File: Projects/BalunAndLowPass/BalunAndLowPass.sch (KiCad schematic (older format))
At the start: 16 parts, among them J1 SMA-J-P-H-ST-EM1, J2 SMA-J-P-H-ST-EM1, J3 SMA-J-P-H-ST-EM1, J4 SMA-J-P-H-ST-EM1, J5 SMA-J-P-H-ST-EM1, J6 SMA-J-P-H-ST-EM1

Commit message: post board review they are all ready to order
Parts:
- added L11, L22: 470nH, Inductor_SMD:L_0805_2012Metric, symbol Device:L
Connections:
- net I_Filtered: now also L11.1; no longer L1.1
- net Q_Filtered: now also L22.1; no longer L2.1
- new net: L1.1, L11.2
- new net: L2.1, L22.2
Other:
- moved on the sheet: C2, C4, J5, J6
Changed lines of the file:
@@
 L Device:C C2
 U 1 1 60232846
-P 5800 2300
-F 0 "C2" H 5915 2346 50  0000 L CNN
-F 1 "160pF" H 5915 2255 50  0000 L CNN
-F 2 "Capacitor_SMD:C_0805_2012Metric" H 5838 2150 50  0001 C CNN
-F 3 "~" H 5800 2300 50  0001 C CNN
-	1    5800 2300
+P 6350 2300
+F 0 "C2" H 6465 2346 50  0000 L CNN
+F 1 "160pF" H 6465 2255 50  0000 L CNN
+F 2 "Capacitor_SMD:C_0805_2012Metric" H 6388 2150 50  0001 C CNN
+F 3 "~" H 6350 2300 50  0001 C CNN
+	1    6350 2300
 	1    0    0    -1
 $EndComp
@@
 	5250 2100 5400 2100
 Wire Wire Line
-	5800 2150 5800 2100
-Wire Wire Line
-	5800 2100 5700 2100
+	6350 2150 6350 2100
 $Comp
 L power:GND #PWR0103
@@
 L power:GND #PWR0104
 U 1 1 602342D8
-P 5800 2500
-F 0 "#PWR0104" H 5800 2250 50  0001 C CNN
-F 1 "GND" H 5805 2327 50  0000 C CNN
-F 2 "" H 5800 2500 50  0001 C CNN
-F 3 "" H 5800 2500 50  0001 C CNN
-	1    5800 2500
+P 6350 2500
+F 0 "#PWR0104" H 6350 2250 50  0001 C CNN
+F 1 "GND" H 6355 2327 50  0000 C CNN
+F 2 "" H 6350 2500 50  0001 C CNN
+F 3 "" H 6350 2500 50  0001 C CNN
+	1    6350 2500
 	1    0    0    -1
 $EndComp
@@
 L Device:C C4
 U 1 1 60244378
-P 5800 1500
-F 0 "C4" H 5915 1546 50  0000 L CNN
-F 1 "160pF" H 5915 1455 50  0000 L CNN
-F 2 "Capacitor_SMD:C_0805_2012Metric" H 5838 1350 50  0001 C CNN
-F 3 "~" H 5800 1500 50  0001 C CNN
-	1    5800 1500
+P 6350 1500
+F 0 "C4" H 6465 1546 50  0000 L CNN
+F 1 "160pF" H 6465 1455 50  0000 L CNN
+F 2 "Capacitor_SMD:C_0805_2012Metric" H 6388 1350 50  0001 C CNN
+F 3 "~" H 6350 1500 50  0001 C CNN
+	1    6350 1500
 	1    0    0    -1
 $EndComp
@@
 	5250 1300 5400 1300
 Wire Wire Line
-	5800 1350 5800 1300
-Wire Wire Line
-	5800 1300 5700 1300
+	6350 1350 6350 1300
 $Comp
 L power:GND #PWR0107
@@
 L power:GND #PWR0108
 U 1 1 60244390
-P 5800 1650
-F 0 "#PWR0108" H 5800 1400 50  0001 C CNN
-F 1 "GND" H 5805 1477 50  0000 C CNN
-F 2 "" H 5800 1650 50  0001 C CNN
-F 3 "" H 5800 1650 50  0001 C CNN
-	1    5800 1650
+P 6350 1650
+F 0 "#PWR0108" H 6350 1400 50  0001 C CNN
+F 1 "GND" H 6355 1477 50  0000 C CNN
+F 2 "" H 6350 1650 50  0001 C CNN
+F 3 "" H 6350 1650 50  0001 C CNN
+	1    6350 1650
 	1    0    0    -1
 $EndComp
@@
 	4600 1300 5250 1300
 Wire Wire Line
-	5800 1300 6450 1300
-Connection ~ 5800 1300
-Wire Wire Line
-	5800 2100 6450 2100
-Connection ~ 5800 2100
-Text Label 6000 1300 0    50   ~ 0
+	6350 1300 7000 1300
+Connection ~ 6350 1300
+Wire Wire Line
+	6350 2100 7000 2100
+Connection ~ 6350 2100
+Text Label 6550 1300 0    50   ~ 0
 Q_Filtered
-Text Label 5950 2100 0    50   ~ 0
+Text Label 6500 2100 0    50   ~ 0
 I_Filtered
 $Comp
@@
 L RandomSMAIFoundOnline:SMA-J-P-H-ST-EM1 J6
 U 1 1 60255A35
-P 6550 2200
-F 0 "J6" H 6390 2286 50  0000 R CNN
-F 1 "SMA-J-P-H-ST-EM1" H 6390 2195 50  0000 R CNN
-F 2 "SAMTEC_SMA-J-P-H-ST-EM1" H 6550 2200 50  0001 L BNN
-F 3 "" H 6550 2200 50  0001 L BNN
-F 4 "Samtec" H 6550 2200 50  0001 L BNN "MANUFACTURER"
-F 5 "G" H 6550 2200 50  0001 L BNN "PARTREV"
-F 6 "Manufacturer Recommendations" H 6550 2200 50  0001 L BNN "STANDARD"
-F 7 "3.675mm" H 6550 2200 50  0001 L BNN "MAXIMUM_PACKAGE_HEIGHT"
-	1    6550 2200
+P 7100 2200
+F 0 "J6" H 6940 2286 50  0000 R CNN
+F 1 "SMA-J-P-H-ST-EM1" H 6940 2195 50  0000 R CNN
+F 2 "SAMTEC_SMA-J-P-H-ST-EM1" H 7100 2200 50  0001 L BNN
+F 3 "" H 7100 2200 50  0001 L BNN
+F 4 "Samtec" H 7100 2200 50  0001 L BNN "MANUFACTURER"
+F 5 "G" H 7100 2200 50  0001 L BNN "PARTREV"
+F 6 "Manufacturer Recommendations" H 7100 2200 50  0001 L BNN "STANDARD"
+F 7 "3.675mm" H 7100 2200 50  0001 L BNN "MAXIMUM_PACKAGE_HEIGHT"
+	1    7100 2200
 	-1   0    0    -1
 $EndComp
@@
 L RandomSMAIFoundOnline:SMA-J-P-H-ST-EM1 J5
 U 1 1 602585ED
-P 6550 1400
-F 0 "J5" H 6390 1486 50  0000 R CNN
-F 1 "SMA-J-P-H-ST-EM1" H 6390 1395 50  0000 R CNN
-F 2 "SAMTEC_SMA-J-P-H-ST-EM1" H 6550 1400 50  0001 L BNN
-F 3 "" H 6550 1400 50  0001 L BNN
-F 4 "Samtec" H 6550 1400 50  0001 L BNN "MANUFACTURER"
-F 5 "G" H 6550 1400 50  0001 L BNN "PARTREV"
-F 6 "Manufacturer Recommendations" H 6550 1400 50  0001 L BNN "STANDARD"
-F 7 "3.675mm" H 6550 1400 50  0001 L BNN "MAXIMUM_PACKAGE_HEIGHT"
-	1    6550 1400
+P 7100 1400
+F 0 "J5" H 6940 1486 50  0000 R CNN
+F 1 "SMA-J-P-H-ST-EM1" H 6940 1395 50  0000 R CNN
+F 2 "SAMTEC_SMA-J-P-H-ST-EM1" H 7100 1400 50  0001 L BNN
+F 3 "" H 7100 1400 50  0001 L BNN
+F 4 "Samtec" H 7100 1400 50  0001 L BNN "MANUFACTURER"
+F 5 "G" H 7100 1400 50  0001 L BNN "PARTREV"
+F 6 "Manufacturer Recommendations" H 7100 1400 50  0001 L BNN "STANDARD"
+F 7 "3.675mm" H 7100 1400 50  0001 L BNN "MAXIMUM_PACKAGE_HEIGHT"
+	1    7100 1400
 	-1   0    0    -1
 $EndComp
@@
 L power:GND #PWR0113
 U 1 1 60259392
-P 6450 2200
-F 0 "#PWR0113" H 6450 1950 50  0001 C CNN
-F 1 "GND" H 6455 2027 50  0000 C CNN
-F 2 "" H 6450 2200 50  0001 C CNN
-F 3 "" H 6450 2200 50  0001 C CNN
-	1    6450 2200
+P 7000 2200
+F 0 "#PWR0113" H 7000 1950 50  0001 C CNN
+F 1 "GND" H 7005 2027 50  0000 C CNN
+F 2 "" H 7000 2200 50  0001 C CNN
+F 3 "" H 7000 2200 50  0001 C CNN
+	1    7000 2200
 	1    0    0    -1
 $EndComp
@@
 L power:GND #PWR0114
 U 1 1 60259CCE
-P 6450 1400
-F 0 "#PWR0114" H 6450 1150 50  0001 C CNN
-F 1 "GND" H 6455 1227 50  0000 C CNN
-F 2 "" H 6450 1400 50  0001 C CNN
-F 3 "" H 6450 1400 50  0001 C CNN
-	1    6450 1400
-	1    0    0    -1
-$EndComp
-Wire Wire Line
-	5800 2500 5800 2450
+P 7000 1400
+F 0 "#PWR0114" H 7000 1150 50  0001 C CNN
+F 1 "GND" H 7005 1227 50  0000 C CNN
+F 2 "" H 7000 1400 50  0001 C CNN
+F 3 "" H 7000 1400 50  0001 C CNN
+	1    7000 1400
+	1    0    0    -1
+$EndComp
+Wire Wire Line
+	6350 2500 6350 2450
 Wire Wire Line
 	1800 2650 1800 2550
+$Comp
+L Device:L L22
+U 1 1 60256776
+P 5950 1300
+F 0 "L22" V 5769 1300 50  0000 C CNN
+F 1 "470nH" V 5860 1300 50  0000 C CNN
+F 2 "Inductor_SMD:L_0805_2012Metric" H 5950 1300 50  0001 C CNN
+F 3 "~" H 5950 1300 50  0001 C CNN
+	1    5950 1300
+	0    1    1    0
+$EndComp
+$Comp
+L Device:L L11
+U 1 1 60256CAA
+P 6000 2100
+F 0 "L11" V 5819 2100 50  0000 C CNN
+F 1 "470nH" V 5910 2100 50  0000 C CNN
+F 2 "Inductor_SMD:L_0805_2012Metric" H 6000 2100 50  0001 C CNN
+F 3 "~" H 6000 2100 50  0001 C CNN
+	1    6000 2100
+	0    1    1    0
+$EndComp
+Wire Wire Line
+	5700 2100 5850 2100
+Wire Wire Line
+	6150 2100 6350 2100
+Wire Wire Line
+	6100 1300 6350 1300
+Wire Wire Line
+	5800 1300 5700 1300
 $EndSCHEMATC

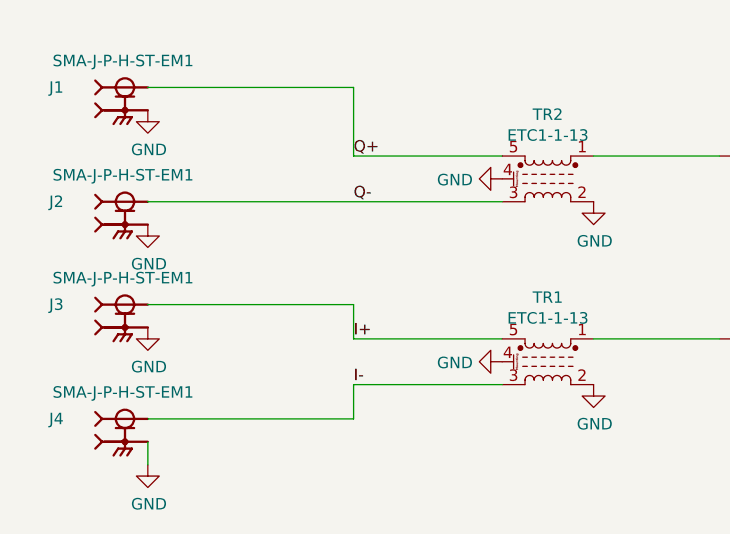
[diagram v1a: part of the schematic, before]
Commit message: Power Detector and power splitter boards designed
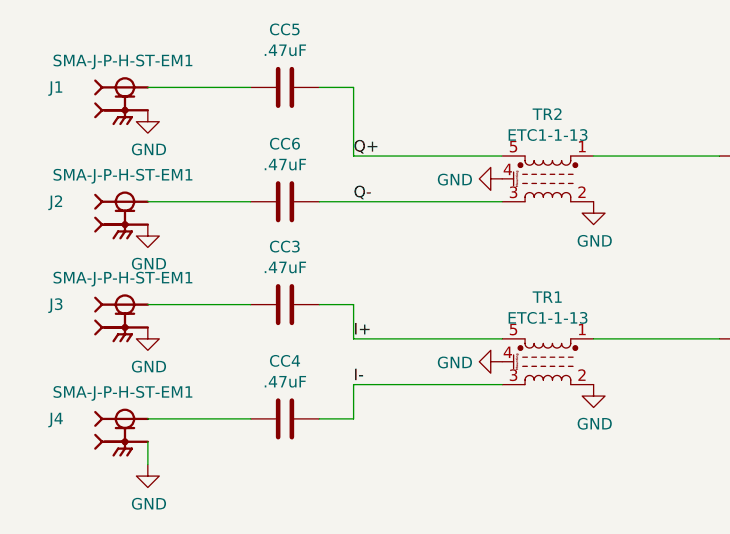
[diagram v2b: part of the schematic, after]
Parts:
- added CC3, CC4, CC5, CC6: .47uF, Capacitor_SMD:C_0805_2012Metric, symbol Device:C
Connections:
- net I+: now also CC3.1; no longer J3.1
- net I-: now also CC4.1; no longer J4.1
- net Q+: now also CC5.1; no longer J1.1
- net Q-: now also CC6.1; no longer J2.1
- new net: CC5.2, J1.1
- new net: CC6.2, J2.1
- new net: CC3.2, J3.1
- new net: CC4.2, J4.1
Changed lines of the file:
@@
 $EndComp
 Wire Wire Line
-	1800 1000 2700 1000
+	1800 1000 2250 1000
 Wire Wire Line
 	2700 1000 2700 1300
 Wire Wire Line
-	1800 1500 3350 1500
+	1800 1500 2250 1500
 Wire Wire Line
-	1800 1950 2700 1950
+	1800 1950 2250 1950
 Wire Wire Line
 	2700 1950 2700 2100
 Wire Wire Line
-	1800 2450 2700 2450
+	1800 2450 2250 2450
 Wire Wire Line
 	2700 2450 2700 2300
@@
 Wire Wire Line
 	5800 1300 5700 1300
+$Comp
+L Device:C CC3
+U 1 1 60513EDB
+P 2400 1950
+F 0 "CC3" V 2148 1950 50  0000 C CNN
+F 1 ".47uF" V 2239 1950 50  0000 C CNN
+F 2 "Capacitor_SMD:C_0805_2012Metric" H 2438 1800 50  0001 C CNN
+F 3 "~" H 2400 1950 50  0001 C CNN
+	1    2400 1950
+	0    1    1    0
+$EndComp
+Wire Wire Line
+	2550 1950 2700 1950
+$Comp
+L Device:C CC4
+U 1 1 6051453A
+P 2400 2450
+F 0 "CC4" V 2148 2450 50  0000 C CNN
+F 1 ".47uF" V 2239 2450 50  0000 C CNN
+F 2 "Capacitor_SMD:C_0805_2012Metric" H 2438 2300 50  0001 C CNN
+F 3 "~" H 2400 2450 50  0001 C CNN
+	1    2400 2450
+	0    1    1    0
+$EndComp
+Wire Wire Line
+	2550 2450 2700 2450
+$Comp
+L Device:C CC5
+U 1 1 60514988
+P 2400 1000
+F 0 "CC5" V 2148 1000 50  0000 C CNN
+F 1 ".47uF" V 2239 1000 50  0000 C CNN
+F 2 "Capacitor_SMD:C_0805_2012Metric" H 2438 850 50  0001 C CNN
+F 3 "~" H 2400 1000 50  0001 C CNN
+	1    2400 1000
+	0    1    1    0
+$EndComp
+Wire Wire Line
+	2550 1000 2700 1000
+$Comp
+L Device:C CC6
+U 1 1 60514E9A
+P 2400 1500
+F 0 "CC6" V 2148 1500 50  0000 C CNN
+F 1 ".47uF" V 2239 1500 50  0000 C CNN
+F 2 "Capacitor_SMD:C_0805_2012Metric" H 2438 1350 50  0001 C CNN
+F 3 "~" H 2400 1500 50  0001 C CNN
+	1    2400 1500
+	0    1    1    0
+$EndComp
+Wire Wire Line
+	2550 1500 3350 1500
 $EndSCHEMATC
